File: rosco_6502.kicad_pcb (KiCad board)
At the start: 4 copper layers, 100 x 100 mm, 50 parts, among them J1 UART_A, J2 UART_B, J3 Conn_01x06, J4 Conn_01x01_Male, J5 DIN41612_02x32_AC, Q1 3.6864MHz, U1 W65C02SxP, U2 MCP130-xxxHxTO, U3 SST39SF010, U4 AS6C4008-55PCN, U5 AS6C62256-55PCN, U6 XR68C681CJTR-F, U7 74HCT174, U8 ATF22V10C-7PX, U9 ATF22V10C-7PX, X1 14MHz

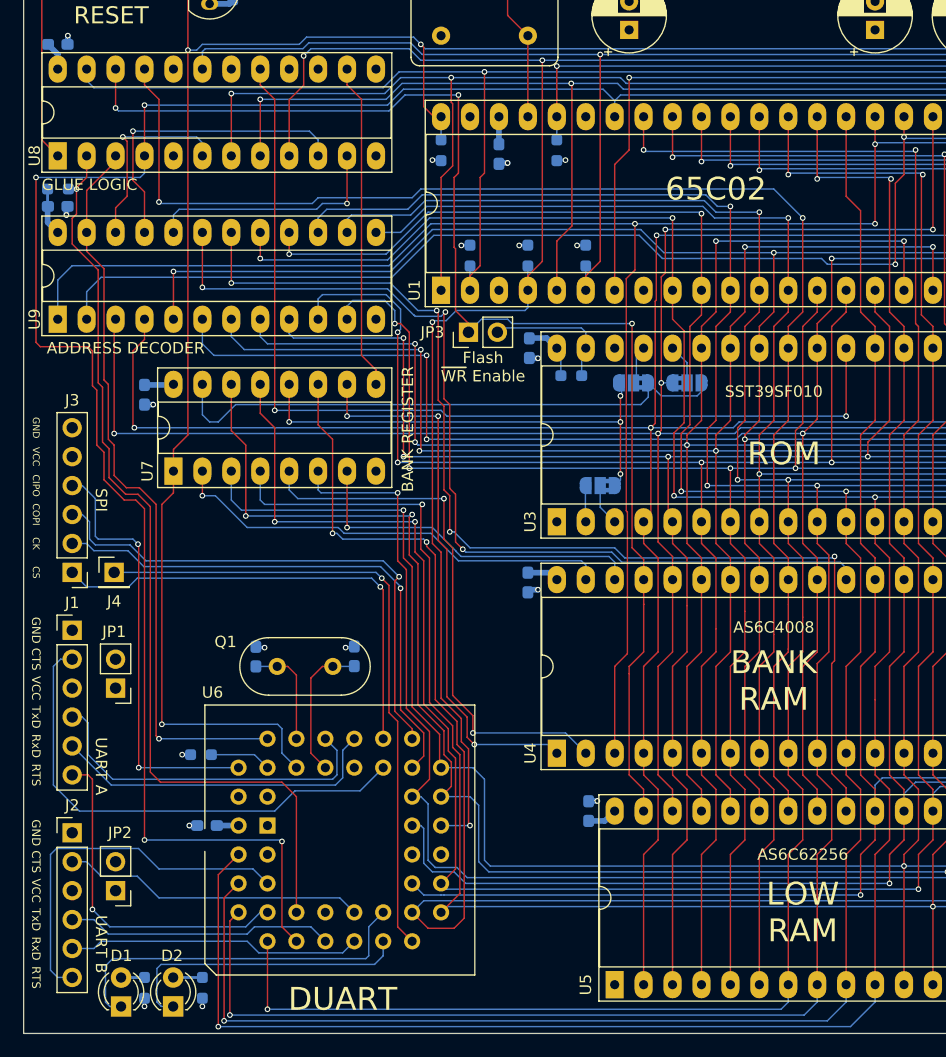
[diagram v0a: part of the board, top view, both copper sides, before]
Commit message: Update for new DUART select logic
And some tidying up
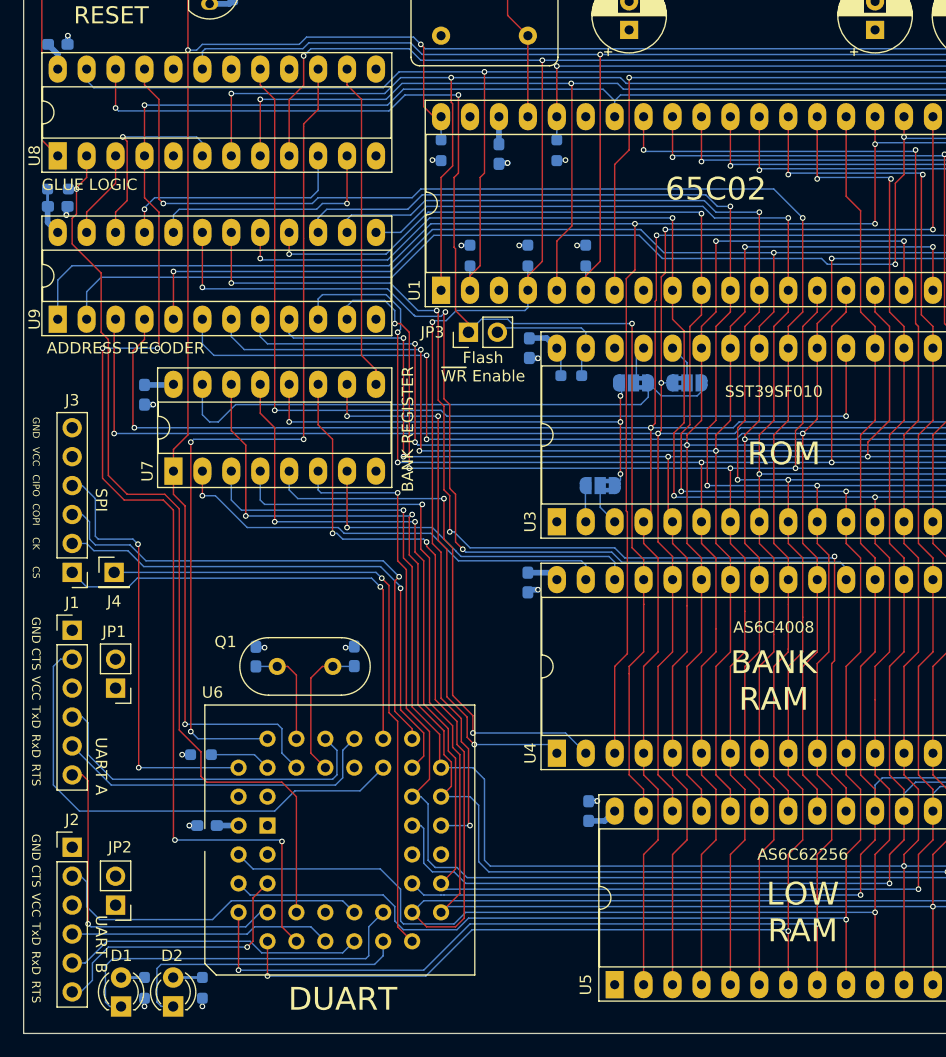
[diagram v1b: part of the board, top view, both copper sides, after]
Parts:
- moved J2 1.27 mm to (41.3, 123.8)
- moved JP2 1.27 mm to (45.1, 128.9)
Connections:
- U6 pad 39: ~{DUASEL} -> ~{DUACS}
- U8 pad 15: unconnected-(U8-IO2-Pad15) -> ~{DUACS}
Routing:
- net ~{DUACS}: track 0.00 -> 75.4 mm, vias 0 -> 3
- net ~{DUASEL}: track 65.0 -> 7.77 mm, vias 1 -> 0
- net A0: track 234.5 -> 219.1 mm
- net A1: track 221.2 -> 208.0 mm
- net R/~{W}: track 198.5 -> 189.6 mm, vias 4 -> 5
- net CTSB: track 32.9 -> 24.2 mm, vias 0 -> 1
- net ~{ROM}: track 27.3 -> 21.1 mm
- net A2: track 216.7 -> 211.4 mm, vias 4 -> 5
- net A3: track 197.8 -> 194.8 mm, vias 4 -> 5
- net RTSB: track 26.6 -> 28.7 mm
- net ~{RESET}: track 177.1 -> 175.1 mm
- net ~{DUADTACK}: track 82.7 -> 81.6 mm
- net CTSA: track 29.9 -> 30.6 mm
- net TXDB: track 25.9 -> 26.4 mm
- net RXDB: track 23.5 -> 23.0 mm

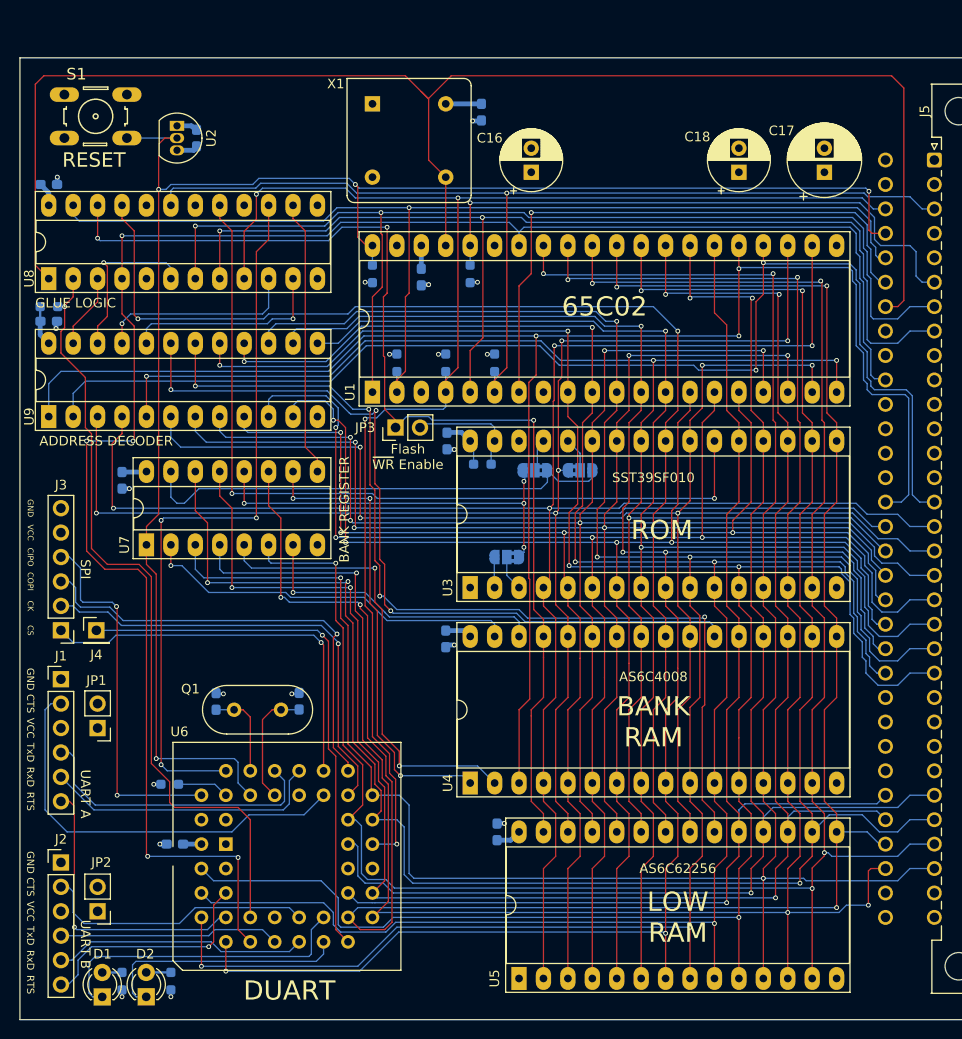
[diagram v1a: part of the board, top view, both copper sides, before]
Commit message: SMD components replaced with THT
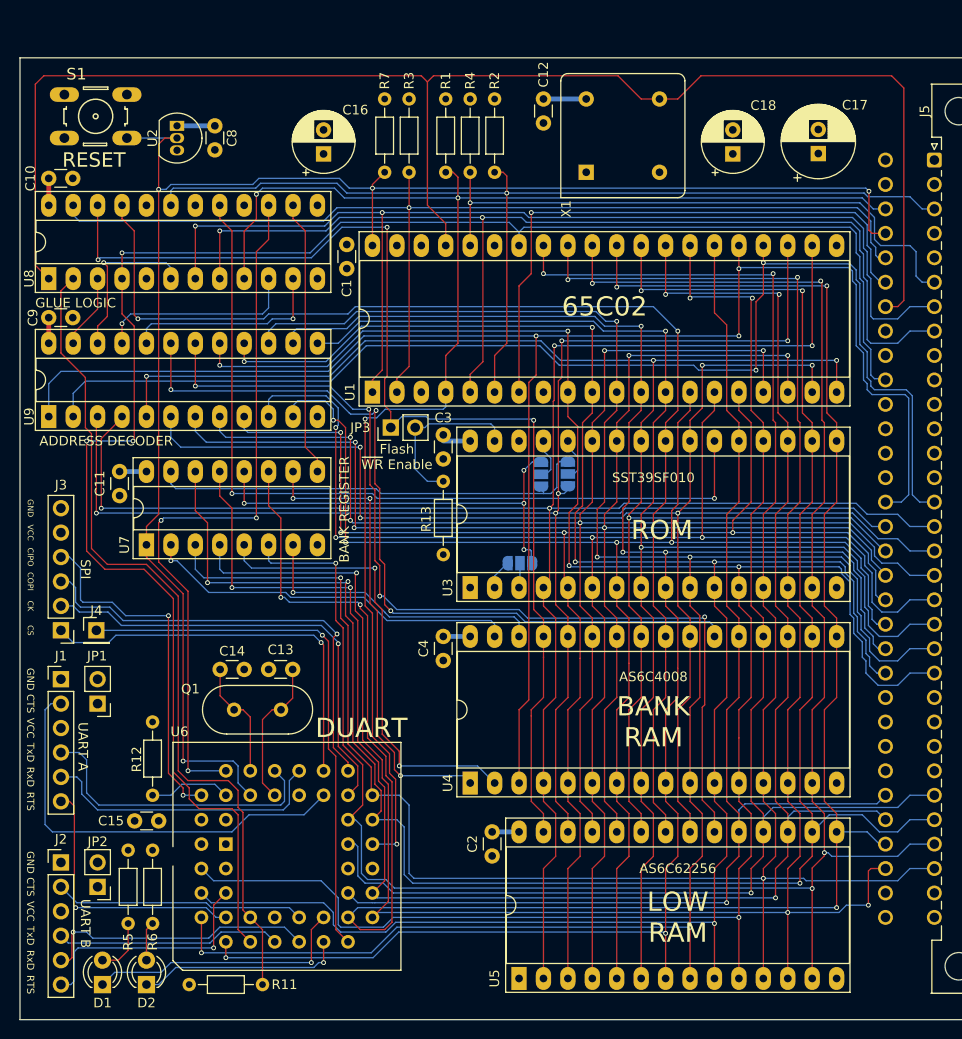
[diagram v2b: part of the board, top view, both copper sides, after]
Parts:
- C1, C10, C11, C12, C13, C14, C15, C2, C3, C4, C8, C9: footprint Capacitor_SMD:C_0603_1608Metric_Pad1.08x0.95mm_HandSolder -> Capacitor_THT:C_Disc_D3.0mm_W1.6mm_P2.50mm; moved to F.Cu
- JP4, JP5, JP6: footprint Jumper:SolderJumper-3_P1.3mm_Bridged2Bar12_RoundedPad1.0x1.5mm -> Jumper:SolderJumper-3_P1.3mm_Open_RoundedPad1.0x1.5mm_NumberLabels
- R1, R11, R12, R13, R2, R3, R4, R5, R6, R7: footprint Resistor_SMD:R_0603_1608Metric_Pad0.98x0.95mm_HandSolder -> Resistor_THT:R_Axial_DIN0204_L3.6mm_D1.6mm_P7.62mm_Horizontal; moved to F.Cu
- moved R11 72.0 mm to (54.6, 136.5)
- moved R3 27.5 mm to (77.5, 44.5)
- moved R1 27.4 mm to (81.3, 44.5)
- moved R2 27.4 mm to (86.4, 44.5)
- moved X1 23.3 mm to (95.9, 52.1), turned to 0 degrees
- moved C16 21.7 mm to (68.6, 50.2)
- moved R7 18.2 mm to (74.9, 44.5), turned to -90 degrees
- moved R4 18.2 mm to (83.8, 44.5), turned to -90 degrees
- moved R6 13.7 mm to (50.8, 122.6), turned to -90 degrees
- moved C1 7.80 mm to (71.0, 62.1)
- moved R12 6.72 mm to (50.8, 109.2), turned to -90 degrees
- moved C12 6.55 mm to (91.4, 47.0)
- moved R5 6.03 mm to (48.3, 130.2), turned to 90 degrees
- moved C15 4.82 mm to (48.9, 119.5)
- moved C13 4.58 mm to (62.9, 103.8), turned to 0 degrees
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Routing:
- net VCC: track 36.3 -> 24.7 mm, vias 8 -> 0
- net GND: track 30.5 -> 19.4 mm, vias 11 -> 0
- net Net-(JP3-B): track 12.0 -> 18.2 mm
- net ~{DUADTACK}: track 81.6 -> 87.4 mm, vias 1 -> 0
- net Net-(D1-K): track 32.7 -> 27.9 mm, vias 0 -> 1
- net Net-(D2-K): track 26.1 -> 21.5 mm, vias 0 -> 1
- net R/~{W}: track 189.6 -> 185.5 mm, vias 5 -> 3
- net Net-(D1-A): track 1.91 -> 5.88 mm
- net BANK4: track 50.3 -> 46.8 mm
- net Net-(U6-*IACK): track 5.40 -> 8.57 mm
- net ~{WR}: track 115.0 -> 118.1 mm
- net BANK5: track 41.6 -> 44.7 mm
- net ~{RESET}: track 175.1 -> 172.0 mm
- net Net-(U6-X2): track 9.46 -> 12.4 mm
- net Net-(U6-X1/CLK): track 12.6 -> 15.4 mm
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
